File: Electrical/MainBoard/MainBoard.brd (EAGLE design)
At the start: 100 x 100 mm, 121 parts, among them IC1 MEGA1284-P, IC2 MCP4922-E/SL, IC3 MCP4921-E/SN, IC4 TL074D, IC5 TL074D, IC6 FT232RL, Q1 BC140-10, Q2 BC160, Q3 BC140-10, Q4 BC160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

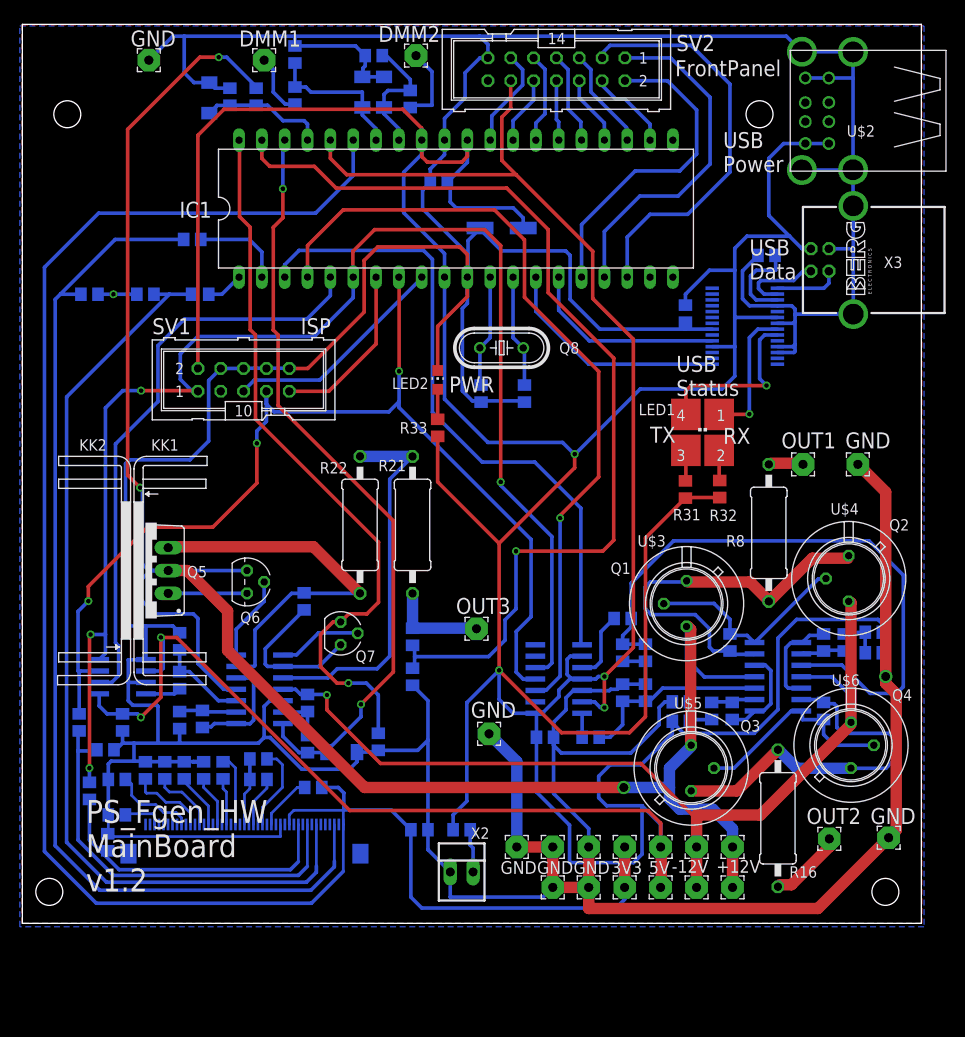
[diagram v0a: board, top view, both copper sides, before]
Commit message: Modified DMM circuit to use DMMRectifier PCB
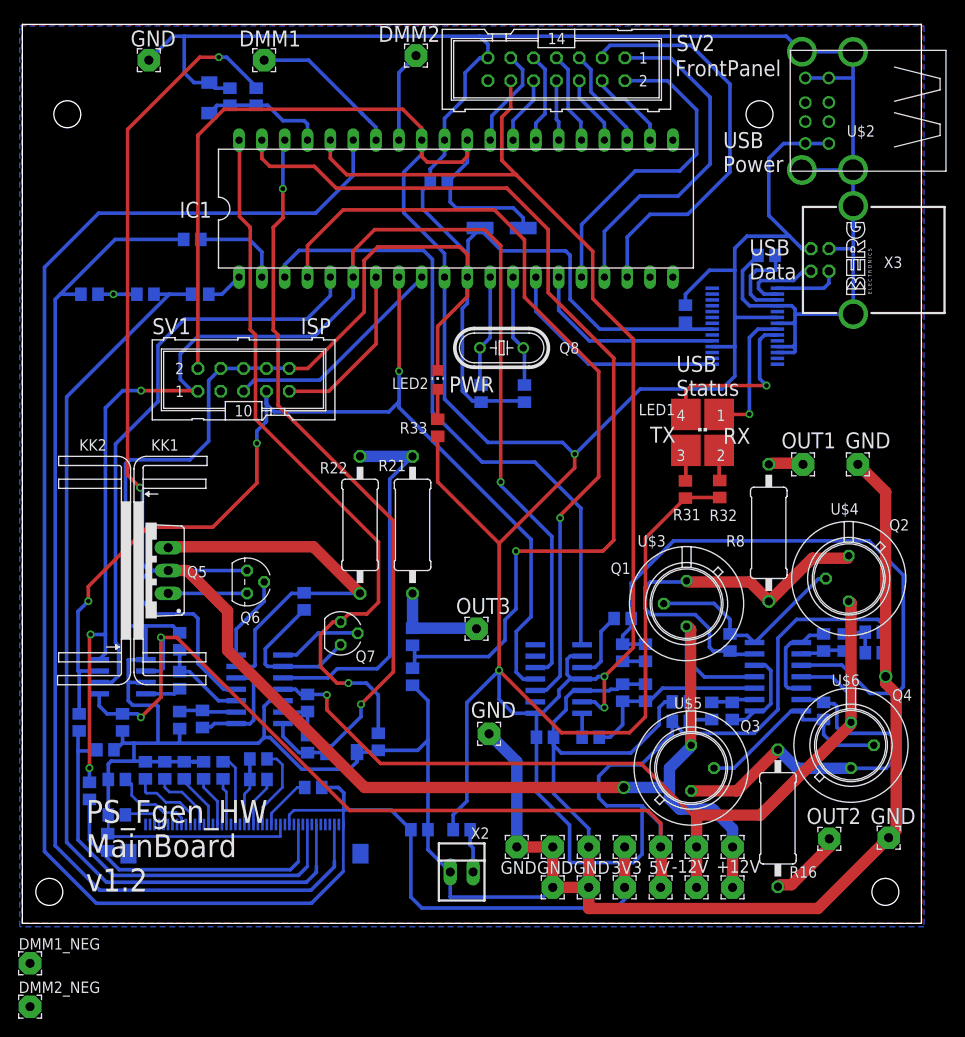
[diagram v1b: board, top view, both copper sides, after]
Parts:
- removed D8, D9: 5V, diode:SOD80C
- removed R35, R37: 100k, OwnDevices:R0805
- removed R36, R38: 24k, OwnDevices:R0805
- added DMM1_NEG, DMM2_NEG: (no value), OwnDevices:2,54/1,0
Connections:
- removed net DVM1_ADC: D8.C, IC1.34, R35.1, R36.2
- removed net DVM2_ADC: D9.C, IC1.33, R37.1, R38.2
- removed net N$40: DMM1.1, R35.2
- removed net N$41: DMM2.1, R37.2
- new net DMM1: DMM1.1, IC1.34
- new net DMM1_NEG: DMM1_NEG.1, IC1.19
- new net DMM2: DMM2.1, IC1.33
- new net DMM2_NEG: DMM2_NEG.1, IC1.20
- net GND: no longer D8.A, D9.A, R36.1, R38.1
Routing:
- net DMM1: track 0.00 -> 16.9 mm
- net DVM1_ADC: track 16.4 -> 0.00 mm
- net DVM2_ADC: track 14.3 -> 0.00 mm
- net GND: track 681.0 -> 666.7 mm
- net DMM2: track 0.00 -> 10.2 mm
- net N$41: track 8.78 -> 0.00 mm
- net N$40: track 6.94 -> 0.00 mm
